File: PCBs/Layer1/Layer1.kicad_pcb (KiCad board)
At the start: 2 copper layers, 90 x 90 mm, 46 parts, among them J1 Screw_Terminal_01x02, J2 Conn_01x12, T1 T60404-E4624-X501, U1 STPM_STPM10BTR, U2 level_shifter, U3 Micro_SD_Shield, U4 DOIT_ESP32_Devkit_v1-MCU_Modu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, Y1 4.194304 MHz

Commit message: Layer1 Ver1.0
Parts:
- moved TP2 17.1 mm to (33.9, 24.1)
- moved TP1 16.0 mm to (38.7, 21.1)
- moved R14 15.0 mm to (85.2, 30.7), turned to 180 degrees
- moved R16 8.81 mm to (92.6, 67.1)
- moved R17 8.81 mm to (85.0, 67.1)
- moved R18 8.81 mm to (87.6, 67.1)
- moved R19 8.81 mm to (90.1, 67.1)
- moved D1 2.16 mm to (57.5, 42.9)
- moved R15 2.16 mm to (55.6, 42.9)
- moved J2 1.88 mm to (99.0, 94.0)
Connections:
- R19 pad 1: MOSI -> /MOSI
- U3 pad 16: MOSI -> Net-(U3-Pad16)
- U3 pad 6: MOSI -> /MOSI
- U4 pad 30: MOSI -> /MOSI
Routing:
- net B3: track 0.00 -> 93.0 mm
- net STPM10_LED: track 3.10 -> 84.3 mm
- net B4: track 0.00 -> 75.4 mm, vias 0 -> 3
- net B2: track 0.00 -> 41.3 mm
- net MOSI: track 37.5 -> 0.00 mm
- net B1: track 0.00 -> 37.2 mm
- net +3V3: track 101.8 -> 133.8 mm, vias 0 -> 1
- net /MOSI: track 0.00 -> 29.1 mm
- net Net-(R11-Pad2): track 13.9 -> 42.6 mm
- net V_IP: track 21.6 -> 34.6 mm
- net I_IN1: track 13.1 -> 23.8 mm
- net /CLK: track 20.1 -> 29.0 mm
- net STPM10_SCS: track 53.6 -> 61.1 mm
- net I_IP1: track 10.3 -> 16.8 mm
- net /MISO: track 24.5 -> 30.6 mm
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- added copper zone on F.Cu, net GND

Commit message: WIP: version 2
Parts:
- added D2: LED_Small, LED_SMD:LED_0603_1608Metric_Pad1.05x0.95mm_HandSolder, F.Cu at (22.1, 63.9)
- added D3: LED_Small, LED_SMD:LED_0603_1608Metric_Pad1.05x0.95mm_HandSolder, F.Cu at (24.6, 63.9)
- added D4: LED_Small, LED_SMD:LED_0603_1608Metric_Pad1.05x0.95mm_HandSolder, F.Cu at (34.8, 63.9)
- added R20: 6.8K, Resistor_SMD:R_0603_1608Metric_Pad1.05x0.95mm_HandSolder, F.Cu at (22.1, 67.8)
- added R21: 6.8K, Resistor_SMD:R_0603_1608Metric_Pad1.05x0.95mm_HandSolder, F.Cu at (24.6, 67.8)
- added R22: 6.8K, Resistor_SMD:R_0603_1608Metric_Pad1.05x0.95mm_HandSolder, F.Cu at (34.8, 67.8)
- C3, C4, C5, C6: footprint Capacitor_SMD:C_1206_3216Metric_Pad1.42x1.75mm_HandSolder -> Capacitor_SMD:C_0603_1608Metric_Pad1.05x0.95mm_HandSolder
- moved C3 16.2 mm to (66.0, 39.4), turned to 270 degrees
- moved U2 10.6 mm to (27.2, 77.0)
- moved C4 10.3 mm to (68.7, 37.0), turned to 0 degrees
- moved C5 7.27 mm to (68.7, 35.5), turned to 180 degrees
- moved C6 4.23 mm to (68.7, 34.0), turned to 180 degrees
- moved C1 2.43 mm to (46.0, 32.7)
- moved C2 2.43 mm to (46.1, 40.7)
- moved R1 2.43 mm to (47.4, 36.8)
- moved Y1 2.13 mm to (51.4, 34.4)
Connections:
- U1 pad 11: Net-(U1-Pad11) -> GND
- U1 pad 12: Net-(U1-Pad12) -> GND
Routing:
- net STPM10_SCL: track 50.2 -> 66.4 mm
- net STPM10_SYN: track 56.4 -> 72.3 mm
- net Net-(C3-Pad1): track 19.2 -> 3.72 mm
- net +3V3: track 133.8 -> 120.8 mm
- net STPM10_SDA: track 42.6 -> 53.8 mm
- net Net-(C5-Pad2): track 13.0 -> 4.70 mm
- net /ESP32_SYN: track 31.7 -> 25.2 mm
- net STPM10_SCS: track 61.1 -> 67.4 mm
- net +5V: track 236.5 -> 242.7 mm
- net Net-(C6-Pad2): track 8.95 -> 4.36 mm
- net Net-(C2-Pad1): track 18.5 -> 14.4 mm
- net /ESP32_SCL: track 26.9 -> 23.6 mm
- net Net-(C1-Pad1): track 16.4 -> 13.9 mm
- net Net-(D3-Pad1): track 0.00 -> 2.20 mm
- net Net-(D4-Pad1): track 0.00 -> 2.19 mm
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
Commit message: WIP: version 2 schematics
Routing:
- removed copper zone on F.Cu, net GND
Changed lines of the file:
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@@
   )
   (setup
-    (last_trace_width 0.381)
+    (last_trace_width 0.25)
     (user_trace_width 0.381)
     (user_trace_width 0.508)
@@
     (solder_mask_min_width 0.25)
     (aux_axis_origin 13 13)
-    (visible_elements FFFFFF7F)
+    (visible_elements FFFFF77F)
     (pcbplotparams
       (layerselection 0x010fc_ffffffff)
@@
   (segment (start 24.638 66.957) (end 24.638 64.756) (width 0.508) (layer F.Cu) (net 70))
   (segment (start 22.098 66.943) (end 22.098 64.77) (width 0.508) (layer F.Cu) (net 71))
-  (zone (net 0) (net_name "") (layer F.Cu) (hatch edge 0.508)
-    (connect_pads (clearance 0.508))
-    (min_thickness 0.254)
-    (keepout (tracks allowed) (vias allowed) (copperpour not_allowed))
-    (fill (arc_segments 16) (thermal_gap 0.508) (thermal_bridge_width 0.508))
-    (polygon
-      (pts
-        (xy 13 13) (xy 13 36) (xy 40 36) (xy 40 25) (xy 52 25)
-        (xy 52 13)
-      )
-    )
-  )
-  (zone (net 2) (net_name GND) (layer F.Cu) (hatch edge 0.508)
-    (connect_pads (clearance 0.508))
-    (min_thickness 0.254)
-    (fill (arc_segments 16) (thermal_gap 0.508) (thermal_bridge_width 0.508))
-    (polygon
-      (pts
-        (xy 13 13) (xy 103 13) (xy 103 103) (xy 13 103)
-      )
-    )
-  )
-  (zone (net 2) (net_name GND) (layer F.Cu) (hatch edge 0.508)
-    (connect_pads (clearance 0.508))
-    (min_thickness 0.254)
-    (fill (arc_segments 16) (thermal_gap 0.508) (thermal_bridge_width 0.508))
-    (polygon
-      (pts
-        (xy 13 13) (xy 103 13) (xy 103 103) (xy 13 103)
-      )
-    )
-  )
 )

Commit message: Layer 1 Ver2, waiting for  review
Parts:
- added C10: 1nF, Capacitor_SMD:C_1806_4516Metric_Pad1.57x1.80mm_HandSolder, F.Cu at (25.5, 32.0)
- added C11: 4700uF, Capacitor_THT:CP_Radial_D12.5mm_P5.00mm, F.Cu at (56.3, 50.7)
- added C9: 470nF 630V, Layer1:C_Rect_L26.5mm_W15.5mm_P22.50mm_MKS4, F.Cu at (38.7, 45.5)
- added D5: 600V 1A, Diode_SMD:D_SMA_Handsoldering, F.Cu at (47.4, 48.8)
- added D6: 600V 1A, Diode_SMD:D_SMA_Handsoldering, F.Cu at (43.4, 48.8)
- added D7: 5.1V, Layer1:SOD-80, F.Cu at (45.4, 42.2)
- added H5: MountingHole, MountingHole:MountingHole_2.7mm_M2.5_DIN965, F.Cu at (100.0, 66.0)
- added H6: MountingHole, MountingHole:MountingHole_2.7mm_M2.5_DIN965, F.Cu at (16.0, 65.0)
- added J3: Screw_Terminal_01x02, TerminalBlock:TerminalBlock_bornier-2_P5.08mm, F.Cu at (22.0, 122.0)
- added J4: Conn_01x06, Connector_PinHeader_2.54mm:PinHeader_1x06_P2.54mm_Vertical, F.Cu at (81.5, 57.0)
- added J5: Conn_01x06, Connector_PinHeader_2.54mm:PinHeader_1x06_P2.54mm_Vertical, F.Cu at (81.4, 65.0)
- added L1: 220uH, Inductor_SMD:L_1812_4532Metric_Pad1.30x3.40mm_HandSolder, F.Cu at (18.2, 35.2)
- added L2: 1uH, Inductor_SMD:L_1812_4532Metric_Pad1.30x3.40mm_HandSolder, F.Cu at (38.9, 32.0)
- added R23: 82R 2W, Resistor_THT:R_Axial_DIN0617_L17.0mm_D6.0mm_P20.32mm_Horizontal, F.Cu at (33.6, 35.4)
- added R24: 0R, Resistor_SMD:R_1206_3216Metric_Pad1.42x1.75mm_HandSolder, F.Cu at (54.0, 16.9)
- added TP5: TestPoint, TestPoint:TestPoint_THTPad_2.0x2.0mm_Drill1.0mm, F.Cu at (72.6, 57.0)
- moved R20 80.0 mm to (100.1, 49.9), turned to 180 degrees
- moved R21 78.4 mm to (100.1, 46.4), turned to 180 degrees
- moved D2 75.4 mm to (96.1, 49.9), turned to 180 degrees
- moved D3 73.6 mm to (96.1, 46.4), turned to 180 degrees
- moved R22 69.8 mm to (100.1, 43.2), turned to 180 degrees
- moved R16 69.5 mm to (23.2, 69.2)
- moved D4 64.7 mm to (96.1, 43.2), turned to 180 degrees
- moved R19 64.4 mm to (25.7, 69.2)
- moved U3 62.8 mm to (29.5, 78.1), turned to 270 degrees
- moved R18 59.3 mm to (28.3, 69.2)
- moved U2 59.3 mm to (86.5, 75.1)
- moved R17 54.3 mm to (30.8, 69.2)
- moved PS1 37.6 mm to (39.0, 92.0), turned to 0 degrees
- moved R14 25.4 mm to (64.3, 16.3), turned to 270 degrees
- moved J2 24.1 mm to (97.0, 118.0)
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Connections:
- net /ESP32_SCL renamed ESP32_SCL
- C1 pad 2: GND -> V_IN
- C2 pad 2: GND -> V_IN
- C3 pad 2: GND -> V_IN
- C4 pad 2: GND -> V_IN
- C5 pad 1: GND -> V_IN
- C6 pad 1: GND -> V_IN
- J2 pad 1: +5V -> +5VD
- J2 pad 12: STPM10_LED -> Net-(J2-Pad12)
- J2 pad 2: GND -> GNDD
- PS1 pad 1: /L -> Net-(J3-Pad1)
- PS1 pad 2: V_IN -> Net-(J3-Pad2)
- PS1 pad 4: GND -> +5VD
- PS1 pad 5: +5V -> GNDD
- R14 pad 2: GND -> V_IN
- R4 pad 1: V_IP -> Net-(R24-Pad2)
- R5 pad 1: V_IP -> Net-(R24-Pad2)
- R7 pad 1: V_IP -> Net-(R24-Pad2)
- U1 pad 11: GND -> Net-(U1-Pad11)
- U1 pad 12: GND -> Net-(U1-Pad12)
- U1 pad 5: GND -> V_IN
- U2 pad 1: /ESP32_SYN -> ESP32_SDA
- U2 pad 12: STPM10_SYN -> STPM10_SDA
- U2 pad 3: GND -> GNDD
- U2 pad 5: /ESP32_SCS -> ESP32_SYN
- U2 pad 6: /ESP32_SDA -> ESP32_SCS
- U2 pad 7: STPM10_SDA -> STPM10_SCS
- U2 pad 8: STPM10_SCS -> STPM10_SYN
- U3 pad 10: GND -> GNDD
- U4 pad 10: /ESP32_SCS -> ESP32_SCS
- U4 pad 13: /ESP32_SYN -> ESP32_SYN
- U4 pad 14: GND -> GNDD
- U4 pad 15: +5V -> +5VD
- U4 pad 8: /ESP32_SDA -> ESP32_SDA
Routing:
- net +5VD: track 0.00 -> 171.6 mm
- net +5V: track 242.7 -> 99.5 mm, vias 1 -> 2
- net V_IN: track 70.9 -> 191.9 mm, vias 0 -> 5
- net STPM10_LED: track 84.3 -> 13.1 mm, vias 0 -> 2
- net B3: track 93.0 -> 25.6 mm
- net B4: track 75.4 -> 25.9 mm, vias 3 -> 0
- net ESP32_RX: track 33.6 -> 76.7 mm
- net ESP32_TX: track 33.8 -> 73.5 mm, vias 0 -> 1
- net /MOSI: track 29.1 -> 66.8 mm
- net ESP32_SYN: track 0.00 -> 35.4 mm
- net Net-(J3-Pad2): track 0.00 -> 32.6 mm
- net +3V3: track 120.8 -> 89.9 mm, vias 1 -> 0
- net STPM10_SCS: track 67.4 -> 38.4 mm
- net Net-(C10-Pad1): track 0.00 -> 28.6 mm
- net ESP32_SCS: track 0.00 -> 26.8 mm
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- added copper zone on F.Cu, net GND
- added copper zone on F.Cu, net GNDD
- added copper zone on B.Cu, net V_IN
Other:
- board size 90 x 90 mm -> 90 x 113 mm

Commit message: WIP add pinheader
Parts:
- added J10: Conn_01x02, Connector_PinHeader_2.54mm:PinHeader_1x02_P2.54mm_Vertical, F.Cu at (18.1, 56.3)
- added J11: Conn_01x02, Connector_PinHeader_2.54mm:PinHeader_1x02_P2.54mm_Vertical, F.Cu at (120.0, 26.3)
- added J12: Conn_01x02, Connector_PinHeader_2.54mm:PinHeader_1x02_P2.54mm_Vertical, F.Cu at (116.2, 41.7)
- added J13: Conn_01x02, Connector_PinHeader_2.54mm:PinHeader_1x02_P2.54mm_Vertical, F.Cu at (130.9, 26.3)
- added J14: Conn_01x02, Connector_PinHeader_2.54mm:PinHeader_1x02_P2.54mm_Vertical, F.Cu at (127.3, 26.3)
- added J15: Conn_01x02, Connector_PinHeader_2.54mm:PinHeader_1x02_P2.54mm_Vertical, F.Cu at (123.6, 26.3)
- added J16: Conn_01x02, Connector_PinHeader_2.54mm:PinHeader_1x02_P2.54mm_Vertical, F.Cu at (130.8, 35.5)
- added J17: Conn_01x02, Connector_PinHeader_2.54mm:PinHeader_1x02_P2.54mm_Vertical, F.Cu at (127.1, 41.7)
- added J6: Conn_01x02, Connector_PinHeader_2.54mm:PinHeader_1x02_P2.54mm_Vertical, F.Cu at (127.1, 35.5)
- added J7: Conn_01x02, Connector_PinHeader_2.54mm:PinHeader_1x02_P2.54mm_Vertical, F.Cu at (119.8, 35.5)
- added J8: Conn_01x02, Connector_PinHeader_2.54mm:PinHeader_1x02_P2.54mm_Vertical, F.Cu at (59.8, 55.4)
- added J9: Conn_01x02, Connector_PinHeader_2.54mm:PinHeader_1x02_P2.54mm_Vertical, F.Cu at (119.8, 41.7)
- moved TP4 66.6 mm to (61.9, -30.0)
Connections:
- C1 pad 2: V_IN -> GNDREF
- C10 pad 2: V_IN -> GNDREF
- C11 pad 1: +5V -> Net-(C11-Pad1)
- C11 pad 2: V_IN -> GNDREF
- C2 pad 2: V_IN -> GNDREF
- C3 pad 2: V_IN -> GNDREF
- C4 pad 2: V_IN -> GNDREF
- C5 pad 1: V_IN -> GNDREF
- C6 pad 1: V_IN -> GNDREF
- C7 pad 2: V_IN -> GNDREF
- C8 pad 1: I_IP1 -> Net-(C8-Pad1)
- C8 pad 2: I_IN1 -> Net-(C8-Pad2)
- D5 pad 1: +5V -> Net-(C11-Pad1)
- D6 pad 2: V_IN -> GNDREF
- D7 pad 1: +5V -> Net-(C11-Pad1)
- D7 pad 2: V_IN -> GNDREF
- J1 pad 2: V_IN -> GNDREF
- L2 pad 1: V_IN -> Net-(J10-Pad1)
- R10 pad 1: I_IP1 -> Net-(C8-Pad1)
- R13 pad 1: I_IN1 -> Net-(C8-Pad2)
- R14 pad 2: V_IN -> GNDREF
- R20 pad 1: STPM10_SYN -> Net-(J12-Pad2)
- R21 pad 1: STPM10_SCL -> Net-(J9-Pad2)
- R22 pad 1: STPM10_SDA -> Net-(J6-Pad1)
- R24 pad 1: V_IP -> Net-(J11-Pad2)
- R5 pad 2: V_IN -> GNDREF
- R6 pad 1: V_IP -> Net-(J11-Pad2)
- R8 pad 2: V_IN -> GNDREF
- R9 pad 2: I_IN1 -> Net-(C8-Pad2)
- RV1 pad 2: V_IN -> GNDREF
- TP1 pad 1: V_IP -> Net-(J11-Pad2)
- TP2 pad 1: V_IN -> GNDREF
- TP3 pad 1: I_IP1 -> Net-(C8-Pad1)
- TP4 pad 1: I_IN1 -> Net-(C8-Pad2)
- U1 pad 15: STPM10_SYN -> Net-(J12-Pad2)
- U1 pad 18: STPM10_SCL -> Net-(J9-Pad2)
- U1 pad 19: STPM10_SDA -> Net-(J6-Pad1)
- U1 pad 3: STPM10_SCS -> Net-(J7-Pad2)
- U1 pad 5: V_IN -> GNDREF
- U2 pad 10: GND -> Net-(J16-Pad1)
- U2 pad 9: +5V -> Net-(J17-Pad2)
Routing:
- net GNDREF: track 0.00 -> 190.3 mm, vias 0 -> 5
- net V_IN: track 191.9 -> 16.3 mm, vias 5 -> 0
- net Net-(J10-Pad2): track 0.00 -> 35.9 mm
- net V_IP: track 54.1 -> 18.8 mm, vias 1 -> 0
- net Net-(J11-Pad2): track 0.00 -> 31.6 mm
- net Net-(C11-Pad1): track 0.00 -> 22.7 mm
- net +5V: track 99.5 -> 77.3 mm
- net I_IN1: track 30.3 -> 12.5 mm
- net I_IP1: track 32.8 -> 15.1 mm
- net Net-(C8-Pad1): track 0.00 -> 15.9 mm
- net Net-(C8-Pad2): track 0.00 -> 14.9 mm

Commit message: Layer1 -- Ready to order
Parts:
- removed J17: Conn_01x02, Connector_PinHeader_2.54mm:PinHeader_1x02_P2.54mm_Vertical
- J4: value Conn_01x06 -> Conn_01x02; footprint Connector_PinHeader_2.54mm:PinHeader_1x06_P2.54mm_Vertical -> Connector_PinHeader_2.54mm:PinHeader_1x02_P2.54mm_Vertical
- moved J13 69.9 mm to (62.2, 39.2), turned to 270 degrees
- moved J11 58.6 mm to (62.2, 36.3), turned to 270 degrees
- moved J14 53.7 mm to (74.5, 36.5), turned to 270 degrees
- moved J15 50.9 mm to (74.5, 39.4), turned to 270 degrees
- moved J6 50.6 mm to (81.5, 57.3)
- moved J16 49.3 mm to (86.5, 57.3)
- moved J9 39.1 mm to (84.0, 57.3)
- moved J7 33.7 mm to (94.2, 57.3)
- moved L2 32.0 mm to (17.5, 55.8), turned to 180 degrees
- moved J12 29.1 mm to (91.6, 57.3)
- moved D1 7.65 mm to (77.2, 58.7)
- moved R15 7.65 mm to (75.4, 58.7)
- moved J4 7.63 mm to (89.1, 57.3), turned to 0 degrees
- moved J10 4.65 mm to (22.7, 55.8), turned to 90 degrees
- moved TP5 1.99 mm to (72.9, 59.0)
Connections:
- J12 pad 1: STPM10_SYN -> Net-(J12-Pad1)
- J12 pad 2: Net-(J12-Pad2) -> STPM10_SYN
- J16 pad 1: Net-(J16-Pad1) -> GND
- J16 pad 2: GND -> GNDB
- J4 pad 1: STPM10_SDA -> 5VB
- J4 pad 2: STPM10_SCL -> +5V
- J5 pad 3: GND -> GNDB
- J5 pad 4: +5V -> 5VB
- J7 pad 1: STPM10_SCS -> Net-(J7-Pad1)
- J7 pad 2: Net-(J7-Pad2) -> STPM10_SCS
- J9 pad 1: STPM10_SCL -> Net-(J9-Pad1)
- J9 pad 2: Net-(J9-Pad2) -> STPM10_SCL
- R20 pad 1: Net-(J12-Pad2) -> Net-(J12-Pad1)
- R21 pad 1: Net-(J9-Pad2) -> Net-(J9-Pad1)
- U1 pad 15: Net-(J12-Pad2) -> Net-(J12-Pad1)
- U1 pad 18: Net-(J9-Pad2) -> Net-(J9-Pad1)
- U1 pad 3: Net-(J7-Pad2) -> Net-(J7-Pad1)
- U2 pad 10: Net-(J16-Pad1) -> Net-(U2-Pad10)
- U2 pad 9: Net-(J17-Pad2) -> 5VB
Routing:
- net Net-(J6-Pad1): track 0.00 -> 61.6 mm, vias 0 -> 2
- net STPM10_SDA: track 68.5 -> 10.2 mm, vias 2 -> 0
- net Net-(J9-Pad1): track 0.00 -> 56.4 mm, vias 0 -> 3
- net STPM10_SCL: track 65.7 -> 10.2 mm, vias 2 -> 0
- net STPM10_SYN: track 58.9 -> 10.2 mm, vias 2 -> 0
- net Net-(J12-Pad1): track 0.00 -> 45.5 mm, vias 0 -> 4
- net Net-(J10-Pad2): track 35.9 -> 0.00 mm
- net STPM10_SCS: track 38.4 -> 10.2 mm, vias 1 -> 0
- net Net-(J7-Pad1): track 0.00 -> 26.2 mm, vias 0 -> 1
- net +5V: track 77.3 -> 60.7 mm
- net GNDB: track 0.00 -> 10.2 mm
- net 5VB: track 0.00 -> 10.2 mm
- net GND: track 13.0 -> 17.1 mm
- net Net-(J10-Pad1): track 0.00 -> 3.02 mm
- net Net-(D1-Pad2): track 1.84 -> 0.00 mm
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- added copper zone on B.Cu, net GNDREF
- removed copper zone on B.Cu, net V_IN
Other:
- outline, holes or cut-outs redrawn
- board text added: "5V"
- board text added: "GND"
- board text added: "I_IN"
- board text added: "I_IP"
- board text added: "LED"
- board text added: "SCL"
- board text added: "SCS"
- board text added: "SDA"
- board text added: "SYN"
- board text added: "V_IN"
- board text added: "V_IP"

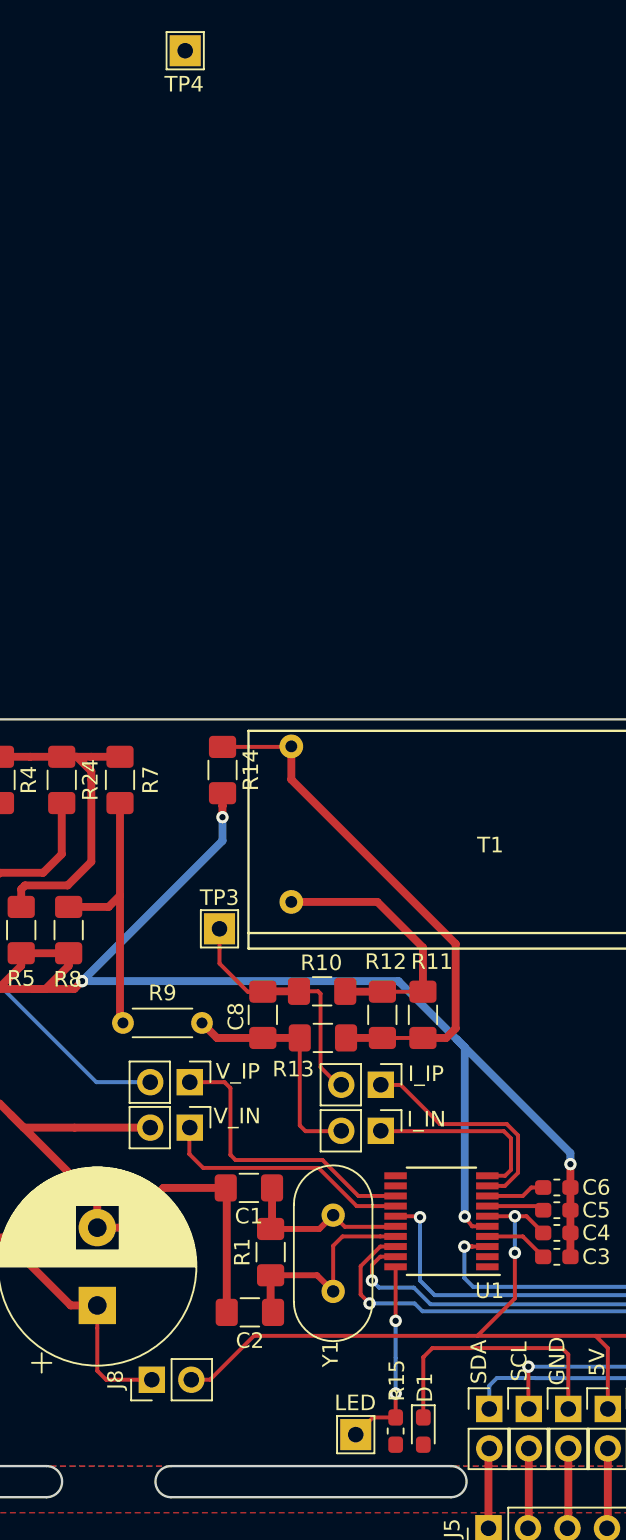
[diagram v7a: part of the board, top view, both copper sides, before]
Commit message: update PCB  Layer1
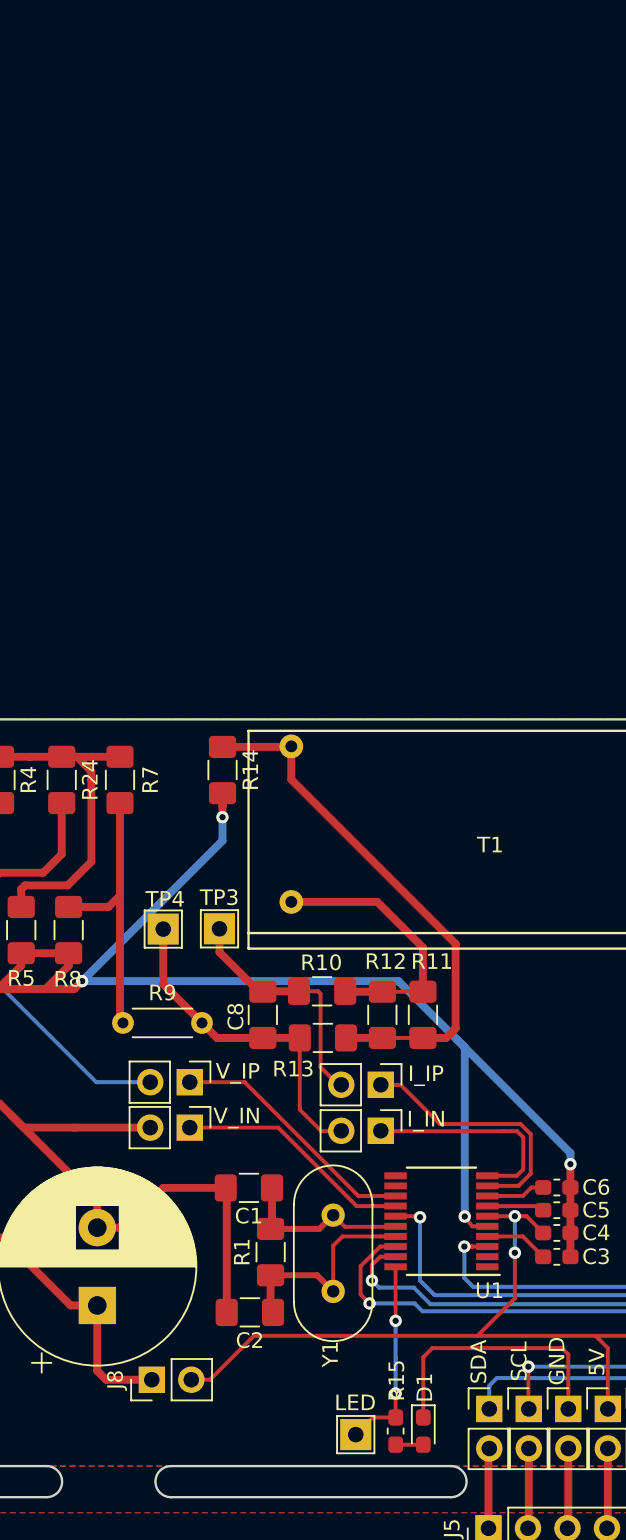
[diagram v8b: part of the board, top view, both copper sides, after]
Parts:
- moved TP4 56.5 mm to (60.5, 26.5)
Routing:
- net Net-(C8-Pad2): track 14.9 -> 21.4 mm
- net V_IP: track 18.8 -> 16.3 mm
- net Net-(D1-Pad2): track 0.00 -> 1.78 mm
- net I_IP1: track 15.1 -> 16.8 mm
- net I_IN1: track 12.5 -> 14.0 mm
- net V_IN: track 16.3 -> 15.3 mm
